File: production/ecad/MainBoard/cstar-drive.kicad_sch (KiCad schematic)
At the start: 62 parts, among them J1 B4B-PH-K-S, J2 B4B-PH-K-S, U1 DRV8842PWPR, U2 DRV8842PWPR, U3 STPS10L25G-TR, U4 STPS10L25G-TR, X1 B2P-VH, X2 B2P-VH

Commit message: "Motor Drive Train Schematic v4"
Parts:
- removed TP10: ~, symbol Connector:TestPoint
- removed TP13, TP14, TP15, TP16, TP17, TP18, TP22, TP23, TP24, TP25, TP26, TP27, TP28, TP29, TP30, TP31, TP32: IN1 MOTOR 1 TP, symbol Connector:TestPoint
- removed TP6: Ch.B Motor 2 TP, symbol Connector:TestPoint
- removed TP9: OUT2 MOTOR 1 TP, symbol Connector:TestPoint
- removed U4: STPS10L25G-TR, D2PAK_STM, symbol STPS10L25G-TR:STPS10L25G-TR
- added J10, J3, J4, J5, J6, J7, J8, J9: Conn_01x03_Pin, symbol Connector:Conn_01x03_Pin
- added TP10, TP6, TP9: IN1 MOTOR 1 TP, symbol Connector:TestPoint
- added TP10: ~, symbol Connector:TestPoint
- added TP6: TestPoint, symbol Connector:TestPoint
- added TP9: OUT2 MOTOR 1 TP, symbol Connector:TestPoint
- added U3, U5, U6: STPS10L25G-TR, D2PAK_STM, symbol STPS10L25G-TR:STPS10L25G-TR
- TP7: value Ch.A Motor 2 TP -> IN1 MOTOR 1 TP
- TP8: value VCC Motor 2 TP -> IN1 MOTOR 1 TP
- renumbered TP11 to TP1, TP12 to TP2, TP19 to TP3, TP20 to TP4, TP21 to TP5, U3 to U4
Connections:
- net GND Motor 1 is gone; now on net GND: J1.2
- net GND Motor 2 is gone; now on net GND: J2.2
- net +12V: now also U3.3 (K), U5.3 (K), U6.3 (K); no longer TP4.1, TP5.1, U1.7 (OUT2), U1.8 (OUT2), U2.7 (OUT2), U2.8 (OUT2), X1.2, X2.2
- net Ch.A Motor 2: now also TP6.1; no longer TP7.1
- net Ch.B Motor 2: now also TP3.1
- net GND: now also TP4.1, TP5.1, U1.7 (OUT2), U1.8 (OUT2), X1.2, X2.2, J10.3 (Pin_3), J3.3 (Pin_3), J4.3 (Pin_3), J5.3 (Pin_3), J6.3 (Pin_3), J7.3 (Pin_3), J8.3 (Pin_3), J9.3 (Pin_3), TP10.1, TP9.1, U3.2 (A), U5.2 (A), U6.2 (A); no longer U2.10 (OUT1), U2.5 (OUT1)
- net IN1 MOTOR 2: now also TP6.1
- net IN2 MOTOR 2: now also TP7.1
- net nFAULT MOTOR 2: now also TP8.1
- net nRESET MOTOR 1: no longer U2.16 (RESET_N)
- net nSLEEP MOTOR 1: no longer U2.17 (SLEEP_N)
- net DECAY MOTOR 1 renamed nDECAY MOTOR 1
- net nDECAY MOTOR 1: no longer U2.19 (DECAY)
- net VCC Motor 1 renamed +3.3V
- net +3.3V: now also J2.1; no longer TP3.1
- removed net VCC Motor 2: J2.1, TP8.1
- new net +3V3: J10.1 (Pin_1), J3.1 (Pin_1), J4.1 (Pin_1), J5.1 (Pin_1), J6.1 (Pin_1), J7.1 (Pin_1), J8.1 (Pin_1), J9.1 (Pin_1)
- new net I0: J3.2 (Pin_2)
- new net I1: J4.2 (Pin_2)
- new net I2: J5.2 (Pin_2)
- new net I3: J6.2 (Pin_2)
- new net I4: J7.2 (Pin_2)
- new net OUT1 MOTOR 2: TP9.1, U2.10 (OUT1), U2.5 (OUT1)
- new net OUT2 MOTOR 2: TP10.1, U2.7 (OUT2), U2.8 (OUT2)
- new net nDECAY: J8.2 (Pin_2)
- new net nDECAY MOTOR 2: U2.19 (DECAY)
- new net nRESET: J9.2 (Pin_2)
- new net nRESET MOTOR 2: U2.16 (RESET_N)
- new net nSLEEP: J10.2 (Pin_2)
- new net nSLEEP MOTOR 2: U2.17 (SLEEP_N)
- no-connect marks 4 -> 6
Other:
- note added: "CURRENT JUMPERS"
- moved on the sheet: C1, C2, C3, C4, C5, C6, J1, R1, R2, R3, R4, R5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

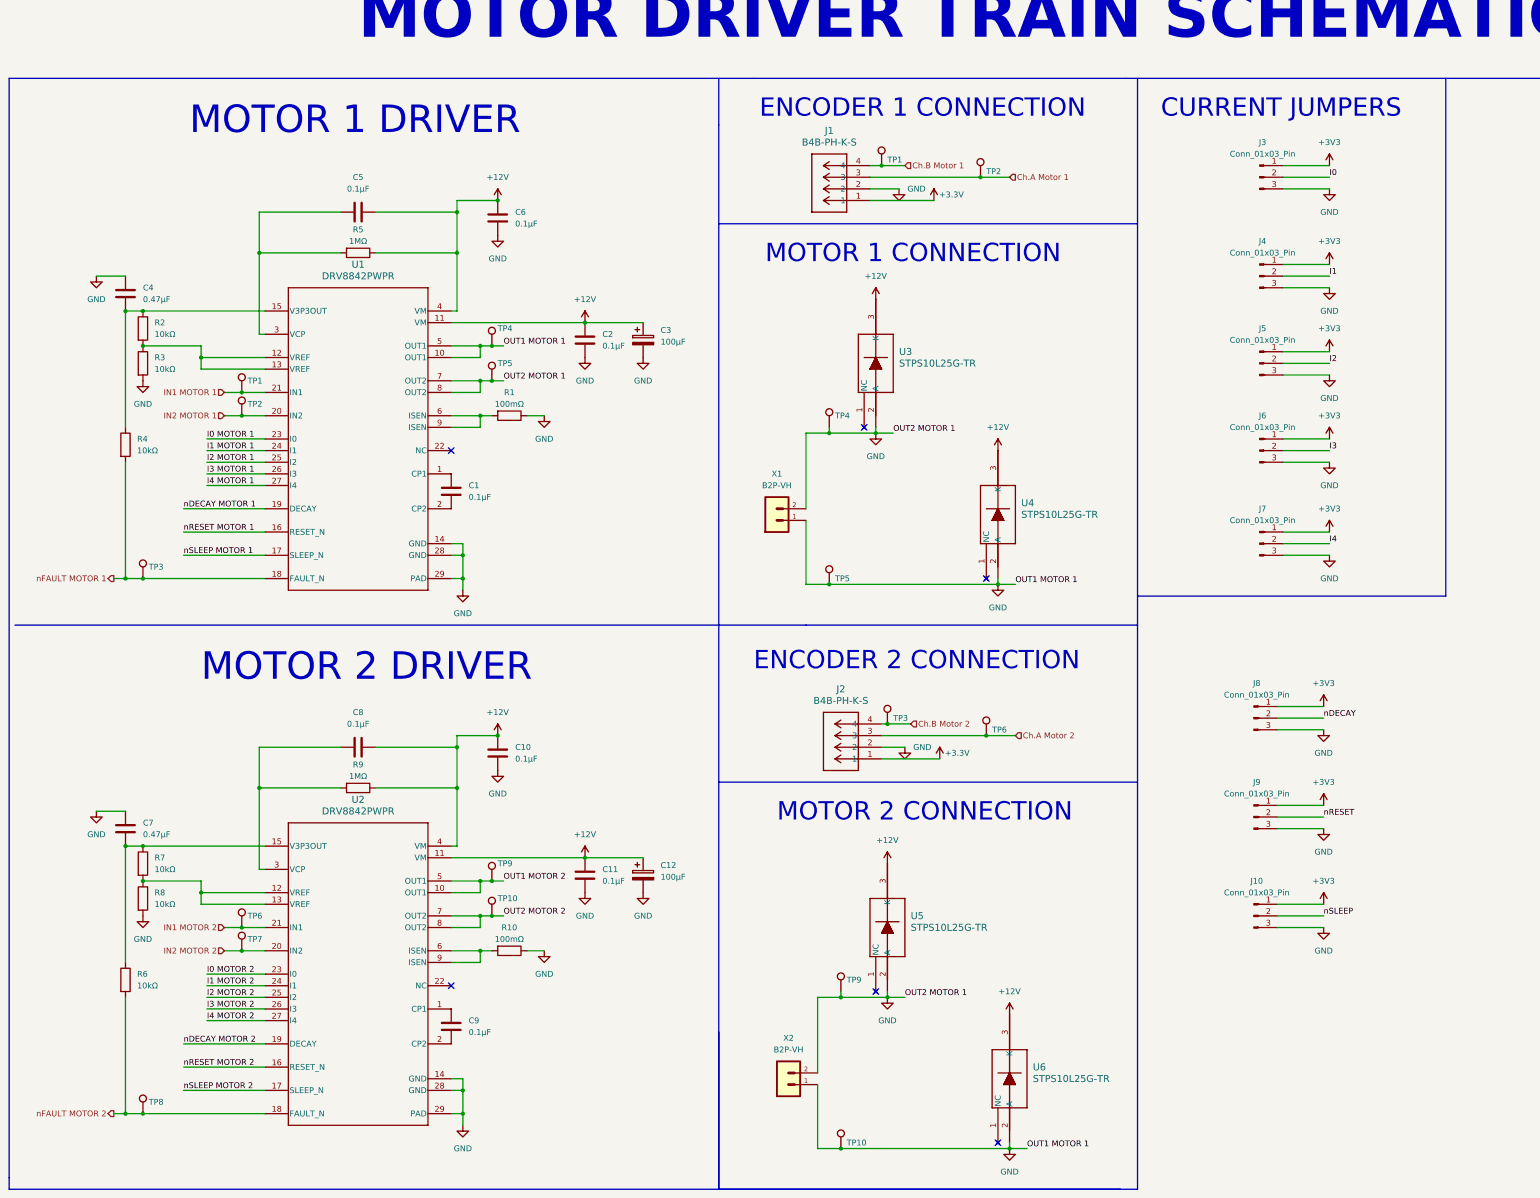
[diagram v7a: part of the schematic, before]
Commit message: "Updated Test Points and Nets"
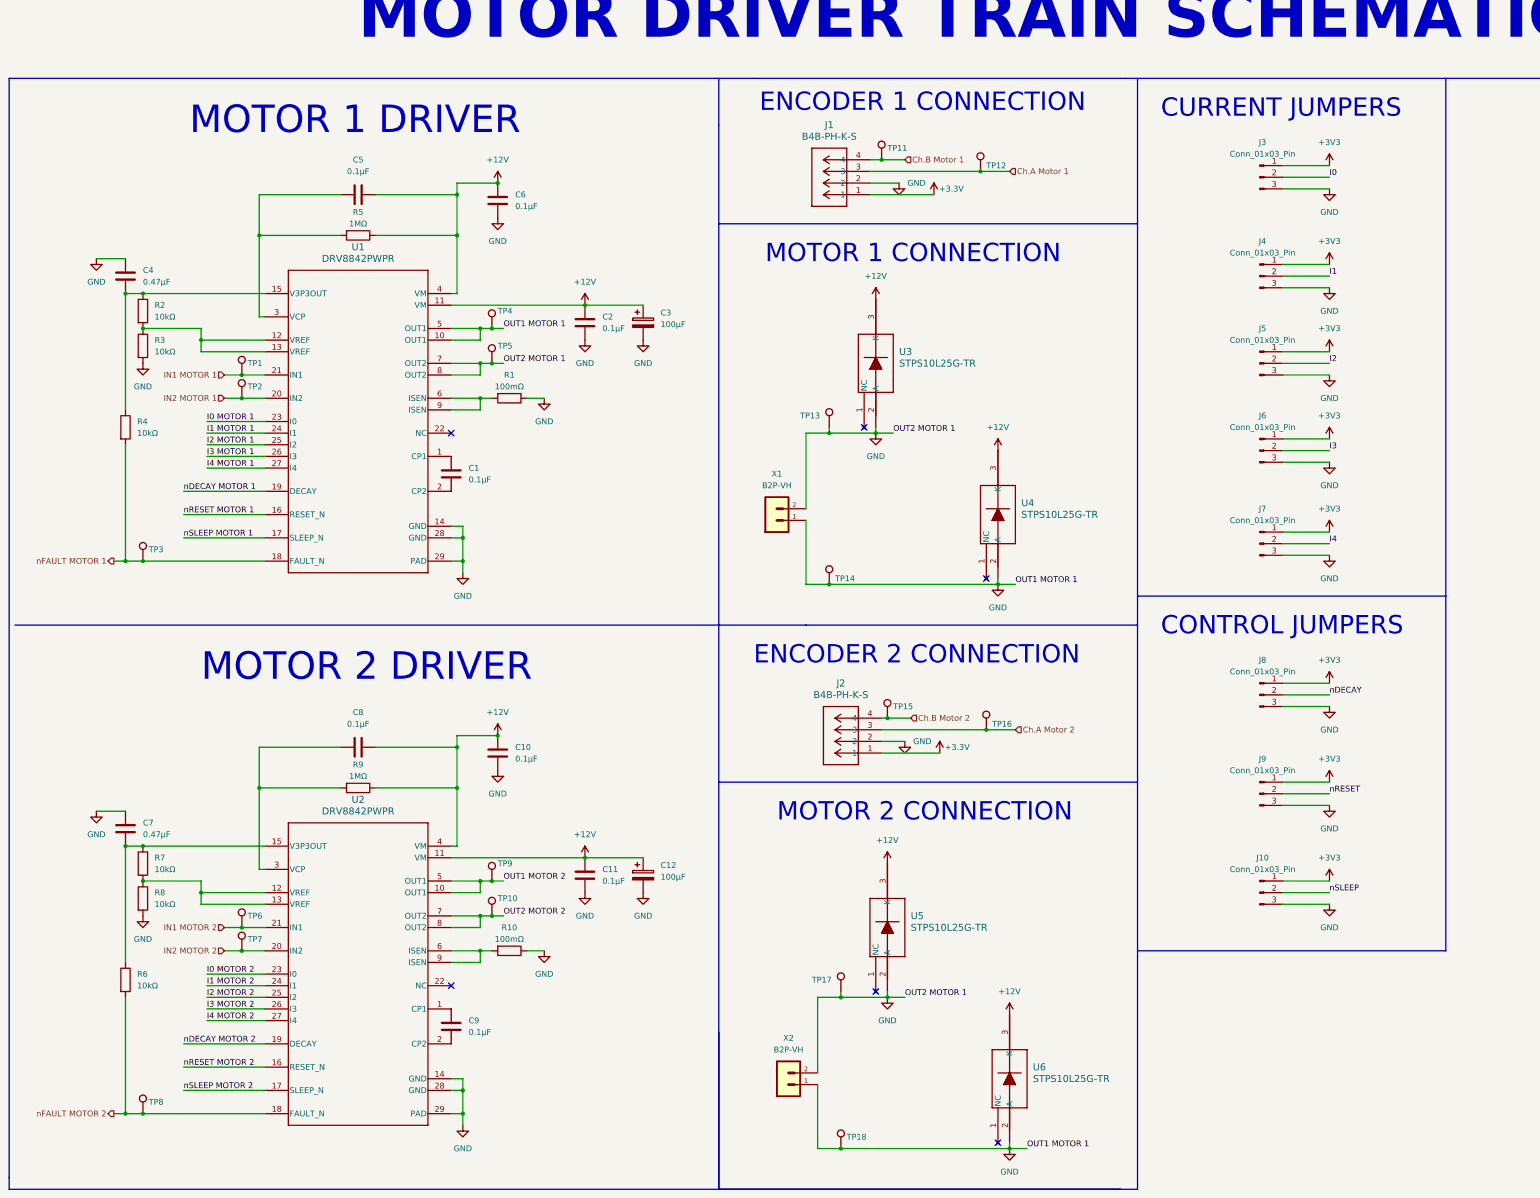
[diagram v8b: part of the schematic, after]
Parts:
- renumbered TP1 to TP11, TP2 to TP12, TP4 to TP13, TP5 to TP14, TP3 to TP15, TP6 to TP16, TP9 to TP17, TP10 to TP18
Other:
- note added: "CONTROL JUMPERS"
- moved on the sheet: C1, C2, C3, C4, C5, C6, J1, J10, J2, J8, J9, R1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
